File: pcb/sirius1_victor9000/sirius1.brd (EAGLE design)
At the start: 56 x 65 mm, 28 parts, among them IC3 STM32F042F4, SW1 324_SW, SW4 324_SW, U1 RJ45

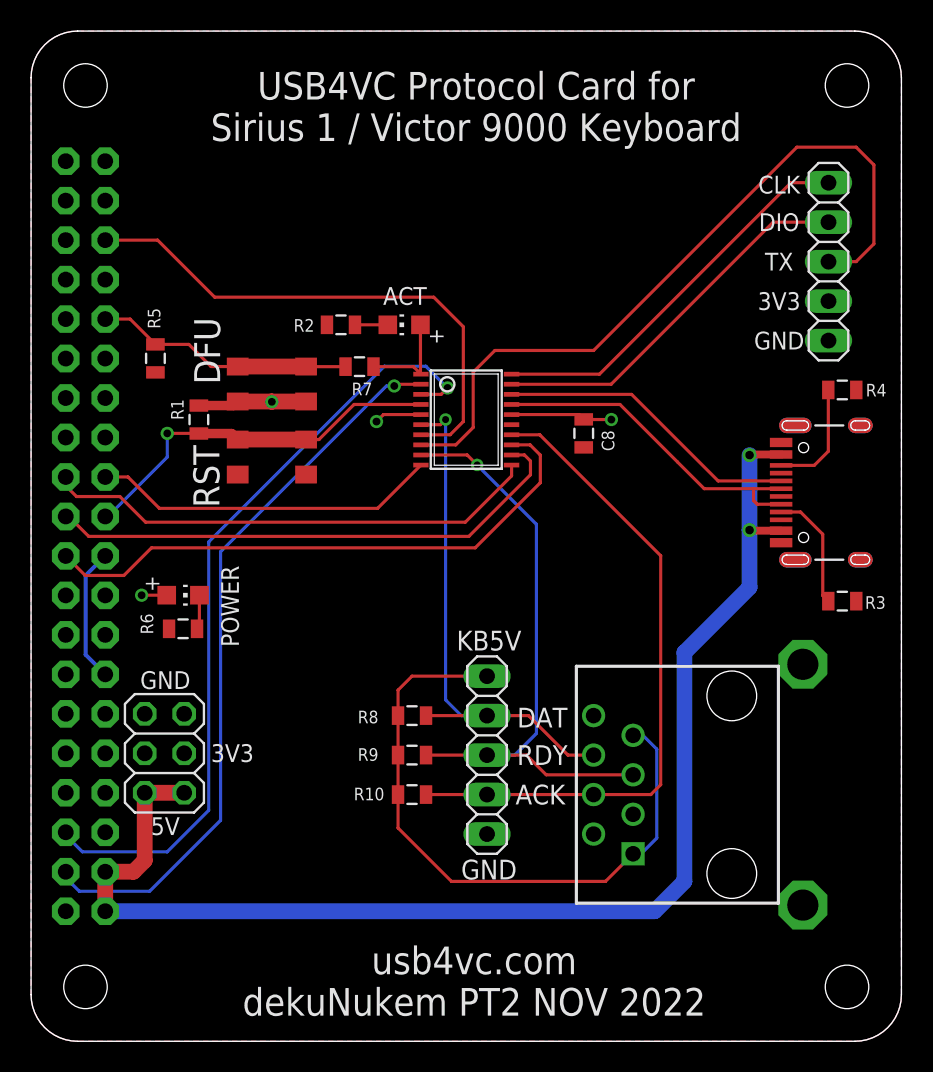
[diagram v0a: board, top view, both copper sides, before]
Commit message: added presence detection
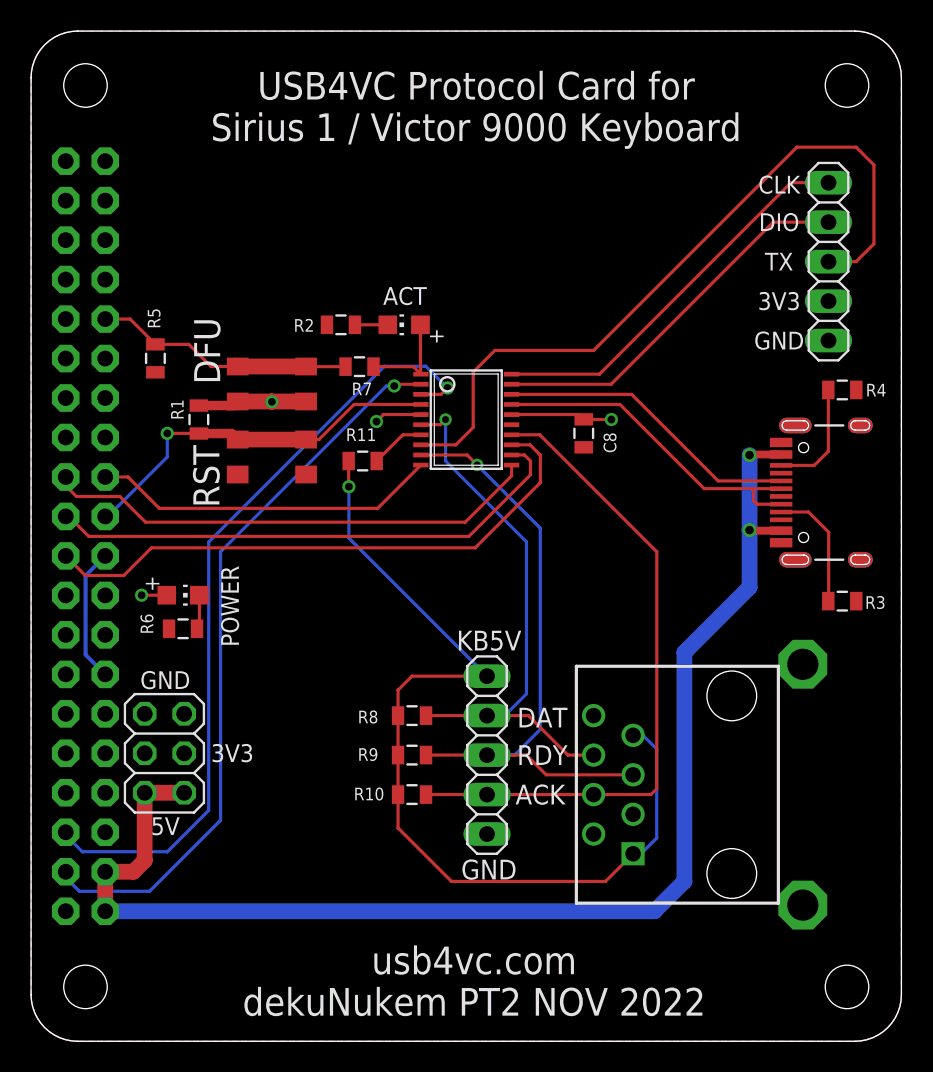
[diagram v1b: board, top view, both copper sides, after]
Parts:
- added R11: 5.1K, SparkFun-Passives:0805
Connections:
- removed net N$12: IC3.7, JP1.36
- new net N$4: IC3.7, R11.1
- net N$27: now also R11.2
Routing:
- net N$12: track 34.5 -> 0.00 mm
- net N$27: track 41.8 -> 59.3 mm, vias 0 -> 1
- net N$4: track 0.00 -> 3.54 mm
- net KBDATA: track 34.7 -> 36.5 mm
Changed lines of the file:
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@@
 </element>
 <element name="C8" library="clock" package="0805@1" value="100nF" x="35.56" y="39.116" smashed="yes" rot="R90">
-<attribute name="NAME" x="37.5285" y="37.973" size="0.8128" layer="25" rot="R90"/>
+<attribute name="NAME" x="37.6555" y="37.846" size="0.8128" layer="25" rot="R90"/>
 </element>
 <element name="JP1" library="adafruit_changed" package="2X20-BIG" value="" x="3.5" y="32.5" smashed="yes" rot="MR90">
@@
 <attribute name="POPULARITY" value="69" x="29.337" y="18.415" size="1.778" layer="27" rot="R270" display="off"/>
 <attribute name="VALUE" x="26.162" y="24.765" size="1.27" layer="27" rot="R270"/>
+</element>
+<element name="R11" library="SparkFun-Passives" package="0805" value="5.1K" x="21.336" y="37.338" smashed="yes" rot="R180">
+<attribute name="NAME" x="22.225" y="39.4335" size="0.8128" layer="25" rot="R180"/>
 </element>
 </elements>
@@
 <contactref element="J4" pad="A5"/>
 <contactref element="R3" pad="1"/>
-<wire x1="49.51" y1="34.056" x2="48.26" y2="34.056" width="0.2032" layer="1"/>
-<wire x1="49.51" y1="34.056" x2="50.938" y2="32.628" width="0.2032" layer="1"/>
-<wire x1="50.938" y1="32.628" x2="50.938" y2="28.68" width="0.2032" layer="1"/>
-<wire x1="50.938" y1="28.68" x2="51.297" y2="28.321" width="0.2032" layer="1"/>
+<wire x1="50.018" y1="34.056" x2="48.26" y2="34.056" width="0.2032" layer="1"/>
+<wire x1="50.018" y1="34.056" x2="51.319" y2="32.755" width="0.2032" layer="1"/>
+<wire x1="51.319" y1="32.755" x2="51.319" y2="28.343" width="0.2032" layer="1"/>
+<wire x1="51.297" y1="28.321" x2="51.319" y2="28.343" width="0.2032" layer="1"/>
 </signal>
 <signal name="N$7">
@@
 <wire x1="26.385" y1="41.625" x2="26.797" y2="42.037" width="0.2032" layer="1"/>
 </signal>
-<signal name="N$12">
-<contactref element="IC3" pad="7"/>
-<contactref element="JP1" pad="36"/>
-<wire x1="25.0822" y1="39.025" x2="26.96" y2="39.025" width="0.2032" layer="1"/>
-<wire x1="26.96" y1="39.025" x2="27.813" y2="39.878" width="0.2032" layer="1"/>
-<wire x1="27.813" y1="39.878" x2="27.813" y2="45.974" width="0.2032" layer="1"/>
-<wire x1="25.908" y1="47.879" x2="11.811" y2="47.879" width="0.2032" layer="1"/>
-<wire x1="11.811" y1="47.879" x2="8.14" y2="51.55" width="0.2032" layer="1"/>
-<wire x1="8.14" y1="51.55" x2="4.77" y2="51.55" width="0.2032" layer="1"/>
-<wire x1="27.813" y1="45.974" x2="25.908" y2="47.879" width="0.2032" layer="1"/>
-</signal>
 <signal name="N$17">
 <contactref element="LED1" pad="C"/>
@@
 <wire x1="33.147" y1="17.145" x2="31.877" y2="18.415" width="0.2032" layer="1"/>
 <wire x1="29.337" y1="18.415" x2="25.411" y2="18.415" width="0.2032" layer="1"/>
-<wire x1="28.702" y1="37.084" x2="32.512" y2="33.274" width="0.2032" layer="16"/>
-<wire x1="32.512" y1="33.274" x2="32.512" y2="19.812" width="0.2032" layer="16"/>
+<wire x1="28.702" y1="37.084" x2="32.766" y2="33.02" width="0.2032" layer="16"/>
+<wire x1="32.766" y1="33.02" x2="32.766" y2="20.066" width="0.2032" layer="16"/>
 <wire x1="31.115" y1="18.415" x2="29.337" y2="18.415" width="0.2032" layer="16"/>
-<wire x1="32.512" y1="19.812" x2="31.115" y2="18.415" width="0.2032" layer="16"/>
+<wire x1="32.766" y1="20.066" x2="31.115" y2="18.415" width="0.2032" layer="16"/>
 </signal>
 <signal name="KBACK">
@@
 <wire x1="36.195" y1="15.875" x2="29.337" y2="15.875" width="0.2032" layer="1"/>
 <wire x1="29.337" y1="15.875" x2="25.411" y2="15.875" width="0.2032" layer="1"/>
-<wire x1="40.513" y1="31.242" x2="40.513" y2="16.51" width="0.2032" layer="1"/>
-<wire x1="32.73" y1="39.025" x2="40.513" y2="31.242" width="0.2032" layer="1"/>
-<wire x1="40.513" y1="16.51" x2="39.878" y2="15.875" width="0.2032" layer="1"/>
+<wire x1="40.259" y1="16.256" x2="39.878" y2="15.875" width="0.2032" layer="1"/>
 <wire x1="39.878" y1="15.875" x2="36.195" y2="15.875" width="0.2032" layer="1"/>
+<wire x1="40.259" y1="31.496" x2="40.259" y2="16.256" width="0.2032" layer="1"/>
+<wire x1="32.73" y1="39.025" x2="40.259" y2="31.496" width="0.2032" layer="1"/>
 </signal>
 <signal name="N$27">
@@
 <wire x1="24.511" y1="23.495" x2="29.337" y2="23.495" width="0.2032" layer="1"/>
 <wire x1="23.611" y1="22.595" x2="24.511" y2="23.495" width="0.2032" layer="1"/>
+<contactref element="R11" pad="2"/>
+<wire x1="20.436" y1="37.338" x2="20.436" y2="35.698" width="0.2032" layer="1"/>
+<wire x1="20.436" y1="35.698" x2="20.447" y2="35.687" width="0.2032" layer="1"/>
+<via x="20.447" y="35.687" extent="1-16" drill="0.5"/>
+<wire x1="20.447" y1="35.687" x2="20.447" y2="32.385" width="0.2032" layer="16"/>
+<wire x1="20.447" y1="32.385" x2="29.337" y2="23.495" width="0.2032" layer="16"/>
 </signal>
 <signal name="KBDATA">
@@
 <wire x1="34.544" y1="18.415" x2="32.004" y2="20.955" width="0.2032" layer="1"/>
 <wire x1="29.337" y1="20.955" x2="25.411" y2="20.955" width="0.2032" layer="1"/>
-<wire x1="26.67" y1="40.005" x2="26.67" y2="21.971" width="0.2032" layer="16"/>
-<wire x1="27.686" y1="20.955" x2="29.337" y2="20.955" width="0.2032" layer="16"/>
-<wire x1="26.67" y1="21.971" x2="27.686" y2="20.955" width="0.2032" layer="16"/>
+<wire x1="26.67" y1="40.005" x2="26.67" y2="37.338" width="0.2032" layer="16"/>
+<wire x1="26.67" y1="37.338" x2="31.877" y2="32.131" width="0.2032" layer="16"/>
+<wire x1="31.877" y1="32.131" x2="31.877" y2="22.352" width="0.2032" layer="16"/>
+<wire x1="30.48" y1="20.955" x2="29.337" y2="20.955" width="0.2032" layer="16"/>
+<wire x1="31.877" y1="22.352" x2="30.48" y2="20.955" width="0.2032" layer="16"/>
 </signal>
 <signal name="N$3">
@@
 <wire x1="48.26" y1="34.556" x2="46.724" y2="34.556" width="0.2032" layer="1"/>
 <wire x1="46.724" y1="34.556" x2="46.482" y2="34.798" width="0.2032" layer="1"/>
-<wire x1="37.892" y1="40.975" x2="41.5925" y2="37.2745" width="0.2032" layer="1"/>
-<wire x1="41.5925" y1="37.2745" x2="43.311" y2="35.556" width="0.2032" layer="1"/>
-<wire x1="43.311" y1="35.556" x2="46.482" y2="35.556" width="0.2032" layer="1"/>
 <wire x1="46.482" y1="35.556" x2="48.26" y2="35.556" width="0.2032" layer="1"/>
 <wire x1="46.482" y1="34.798" x2="46.482" y2="35.556" width="0.2032" layer="1"/>
+<wire x1="43.311" y1="35.556" x2="46.482" y2="35.556" width="0.2032" layer="1"/>
+<wire x1="37.892" y1="40.975" x2="43.311" y2="35.556" width="0.2032" layer="1"/>
 </signal>
 <signal name="N$14">
@@
 <wire x1="30.9178" y1="41.625" x2="38.639" y2="41.625" width="0.2032" layer="1"/>
 </signal>
+<signal name="N$4">
+<contactref element="R11" pad="1"/>
+<contactref element="IC3" pad="7"/>
+<wire x1="25.0822" y1="39.025" x2="23.923" y2="39.025" width="0.2032" layer="1"/>
+<wire x1="23.923" y1="39.025" x2="22.236" y2="37.338" width="0.2032" layer="1"/>
+</signal>
 </signals>
